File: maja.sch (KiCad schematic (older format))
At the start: 54 parts, among them J1 USB, K1 CONN_3, P1 JTAG, P2 CONN_8, SW1 RESET, SW2 BTN, SW3 BTN, U1 CC2538, U2 TPS70933, U3 Antenna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

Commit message: Sync
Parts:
- C19, C20: value C -> 18pF
- C23, C24: value C -> 1pF
- C26: value C -> 1.2pF
- L1, L2, L3: value INDUCTOR -> 2nH
- L4: value INDUCTOR -> 3.3nH
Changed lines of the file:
@@
 P 8000 5400
 F 0 "C19" H 8000 5500 40  0000 L CNN
-F 1 "C" H 8006 5315 40  0000 L CNN
+F 1 "18pF" H 8006 5315 40  0000 L CNN
 F 2 "" H 8038 5250 30  0000 C CNN
 F 3 "" H 8000 5400 60  0000 C CNN
@@
 P 8000 5700
 F 0 "C20" H 8000 5800 40  0000 L CNN
-F 1 "C" H 8006 5615 40  0000 L CNN
+F 1 "18pF" H 8006 5615 40  0000 L CNN
 F 2 "" H 8038 5550 30  0000 C CNN
 F 3 "" H 8000 5700 60  0000 C CNN
@@
 P 8600 5100
 F 0 "C23" H 8600 5200 40  0000 L CNN
-F 1 "C" H 8606 5015 40  0000 L CNN
+F 1 "1pF" H 8606 5015 40  0000 L CNN
 F 2 "" H 8638 4950 30  0000 C CNN
 F 3 "" H 8600 5100 60  0000 C CNN
@@
 P 8600 6100
 F 0 "L1" V 8550 6100 40  0000 C CNN
-F 1 "INDUCTOR" V 8700 6100 40  0000 C CNN
+F 1 "2nH" V 8700 6100 40  0000 C CNN
 F 2 "" H 8600 6100 60  0000 C CNN
 F 3 "" H 8600 6100 60  0000 C CNN
@@
 P 9100 5400
 F 0 "L2" V 9050 5400 40  0000 C CNN
-F 1 "INDUCTOR" V 9200 5400 40  0000 C CNN
+F 1 "2nH" V 9200 5400 40  0000 C CNN
 F 2 "" H 9100 5400 60  0000 C CNN
 F 3 "" H 9100 5400 60  0000 C CNN
@@
 P 9000 5700
 F 0 "C24" H 9000 5800 40  0000 L CNN
-F 1 "C" H 9006 5615 40  0000 L CNN
+F 1 "1pF" H 9006 5615 40  0000 L CNN
 F 2 "" H 9038 5550 30  0000 C CNN
 F 3 "" H 9000 5700 60  0000 C CNN
@@
 P 9950 5550
 F 0 "L3" V 9900 5550 40  0000 C CNN
-F 1 "INDUCTOR" V 10050 5550 40  0000 C CNN
+F 1 "2nH" V 10050 5550 40  0000 C CNN
 F 2 "" H 9950 5550 60  0000 C CNN
 F 3 "" H 9950 5550 60  0000 C CNN
@@
 P 10350 5900
 F 0 "C26" H 10350 6000 40  0000 L CNN
-F 1 "C" H 10356 5815 40  0000 L CNN
+F 1 "1.2pF" H 10356 5815 40  0000 L CNN
 F 2 "" H 10388 5750 30  0000 C CNN
 F 3 "" H 10350 5900 60  0000 C CNN
@@
 P 10650 5250
 F 0 "L4" V 10600 5250 40  0000 C CNN
-F 1 "INDUCTOR" V 10750 5250 40  0000 C CNN
+F 1 "3.3nH" V 10750 5250 40  0000 C CNN
 F 2 "" H 10650 5250 60  0000 C CNN
 F 3 "" H 10650 5250 60  0000 C CNN

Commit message: Finished routing more or less, it is a real pain and uses much too much vias. We have to optimize this if possible
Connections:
- net at C13.1, U1.32 (DVDD_REG): no longer C10.1, U1.56 (DCOUPL)
- new net: C10.1, U1.56 (DCOUPL)
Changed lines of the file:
@@
 Wire Wire Line
 	3000 4300 3000 4450
-Connection ~ 3000 3300
-Wire Wire Line
-	4700 3300 3000 3300
 Wire Wire Line
 	6650 2700 7650 2700
@@
 	8200 1200 8850 1200
 Connection ~ 8400 1200
-Wire Wire Line
-	3000 2300 4700 2300
-Wire Wire Line
-	3000 2300 3000 3900
-Connection ~ 3650 2300
 Wire Wire Line
 	3650 2700 3650 2800
@@
 Wire Wire Line
 	6800 5000 6800 4900
+Wire Wire Line
+	3650 2300 4700 2300
+Wire Wire Line
+	4700 3300 3000 3300
+Wire Wire Line
+	3000 3300 3000 3900
 $EndSCHEMATC

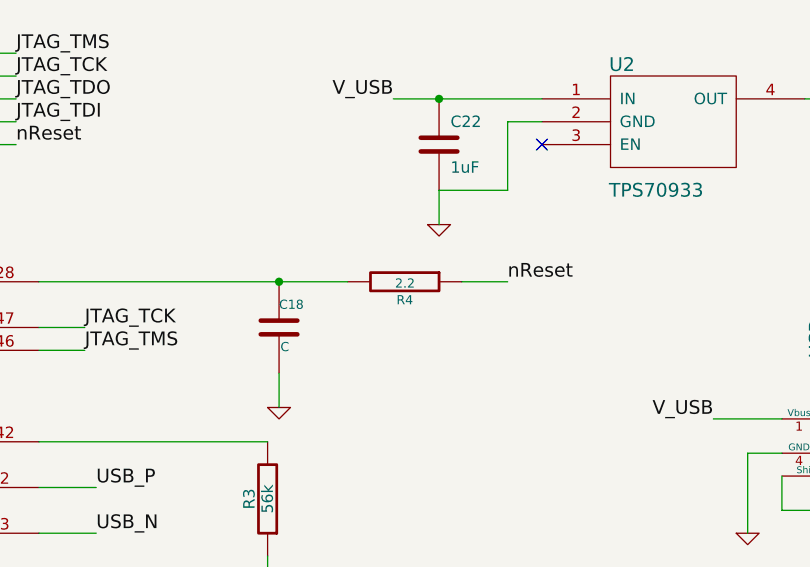
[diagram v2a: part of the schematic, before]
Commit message: Change quartz
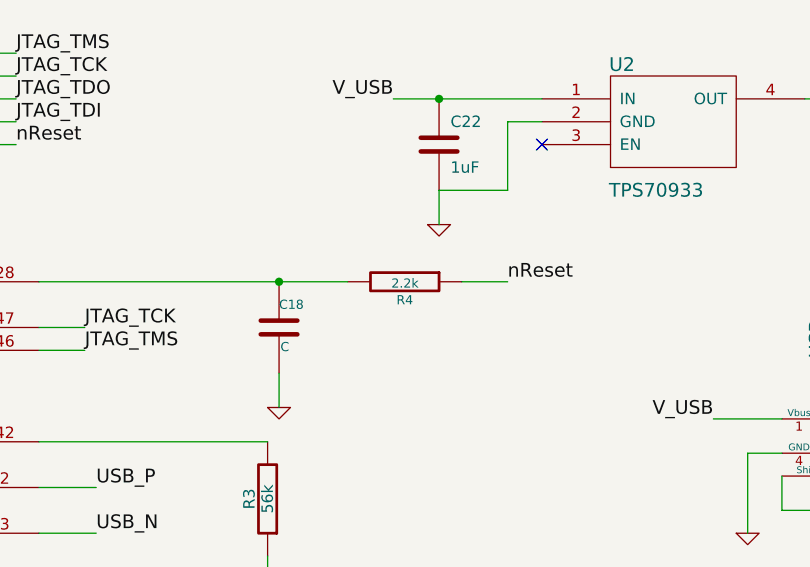
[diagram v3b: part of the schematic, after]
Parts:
- R4: value 2.2 -> 2.2k
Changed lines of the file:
@@
 P 8250 2000
 F 0 "R4" V 8330 2000 40  0000 C CNN
-F 1 "2.2" V 8257 2001 40  0000 C CNN
+F 1 "2.2k" V 8257 2001 40  0000 C CNN
 F 2 "" V 8180 2000 30  0000 C CNN
 F 3 "" H 8250 2000 30  0000 C CNN
